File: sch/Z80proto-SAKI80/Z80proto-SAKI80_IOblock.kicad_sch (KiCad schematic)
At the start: 40 parts, among them SW101 RESET, U101 LMC555, U14 AC541, U15 HC139, U17 TD62783, U18 TD62083, U21 23LC512, U4 HC138

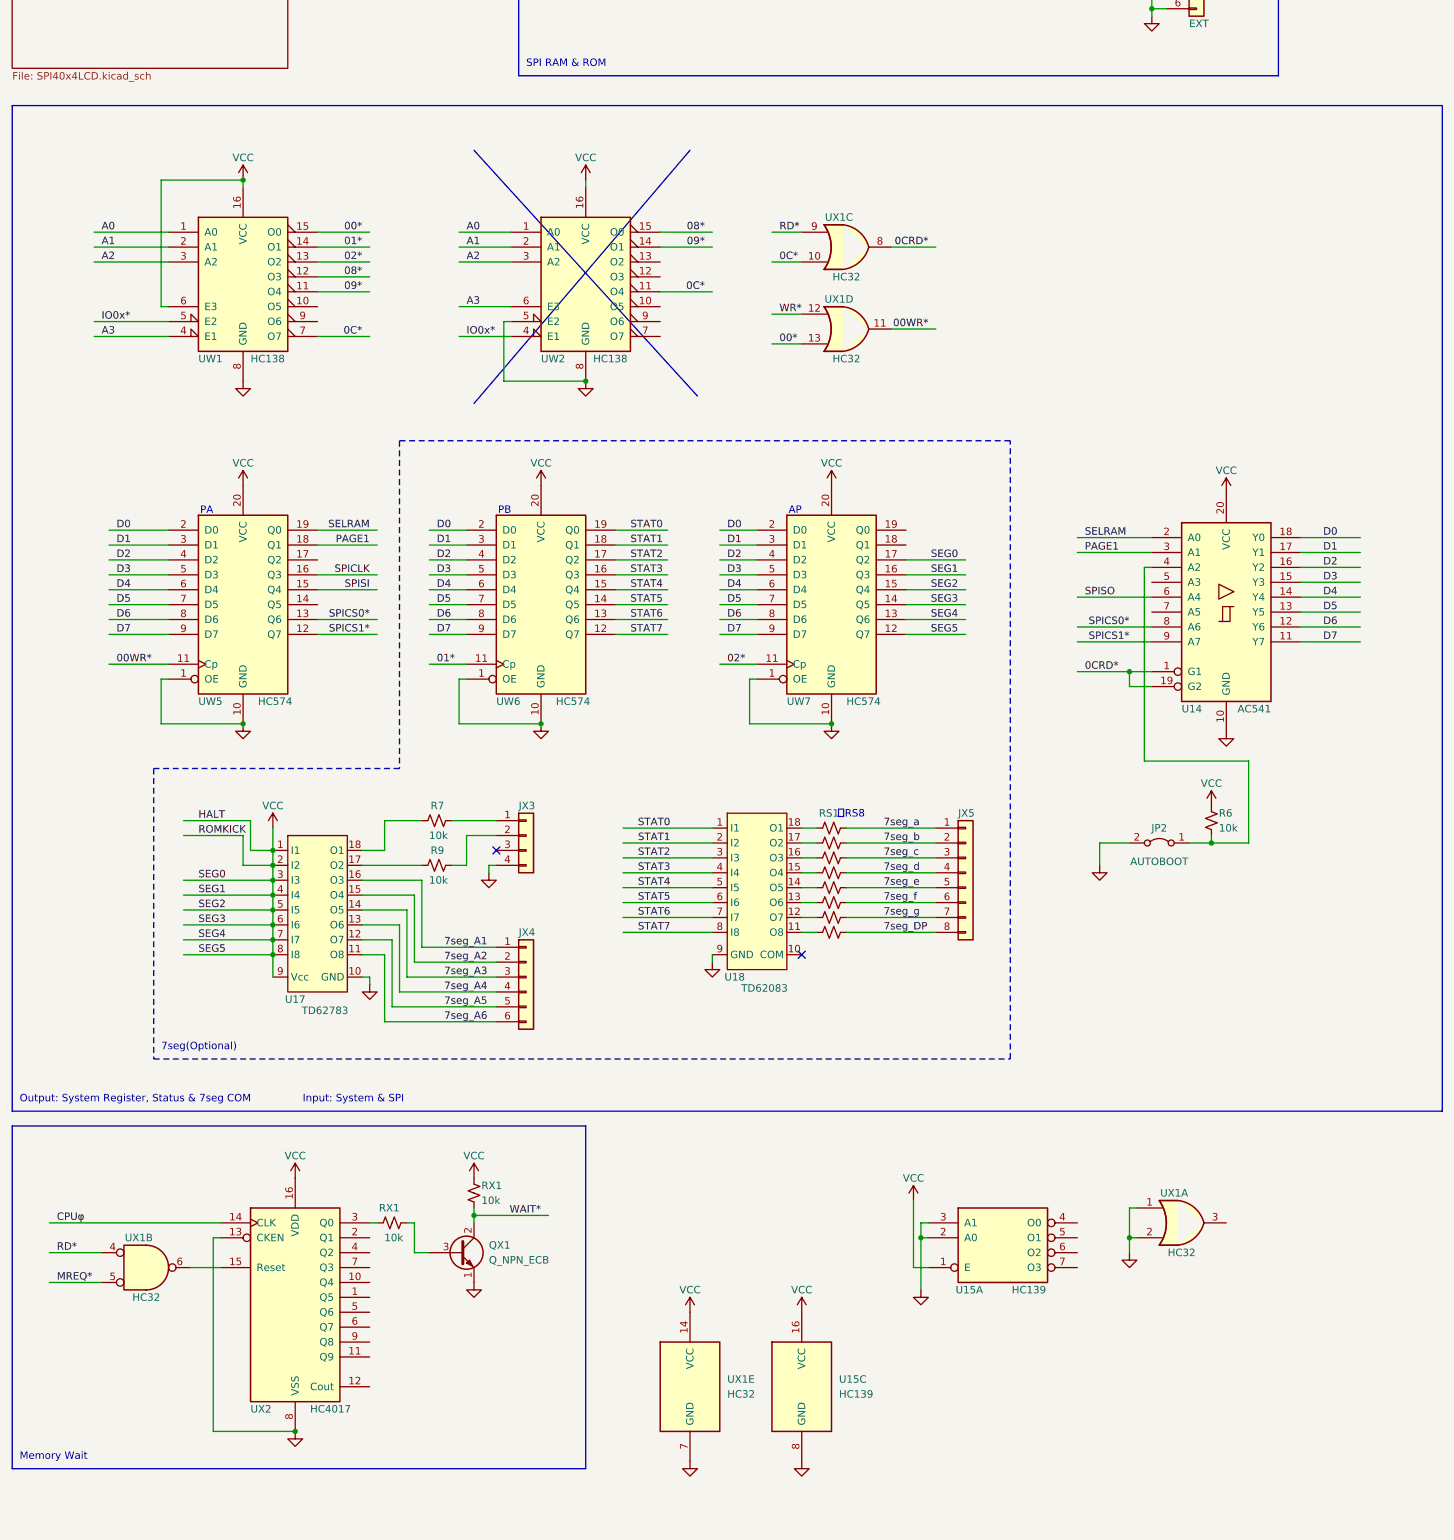
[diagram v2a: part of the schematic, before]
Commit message: Add Async. FIFO support(EXPERIMENTAL)
Add FT245R Asynchronous FIFO support(EXPERIMENTAL)
change environment MiniLoader(zcc->sdcc)
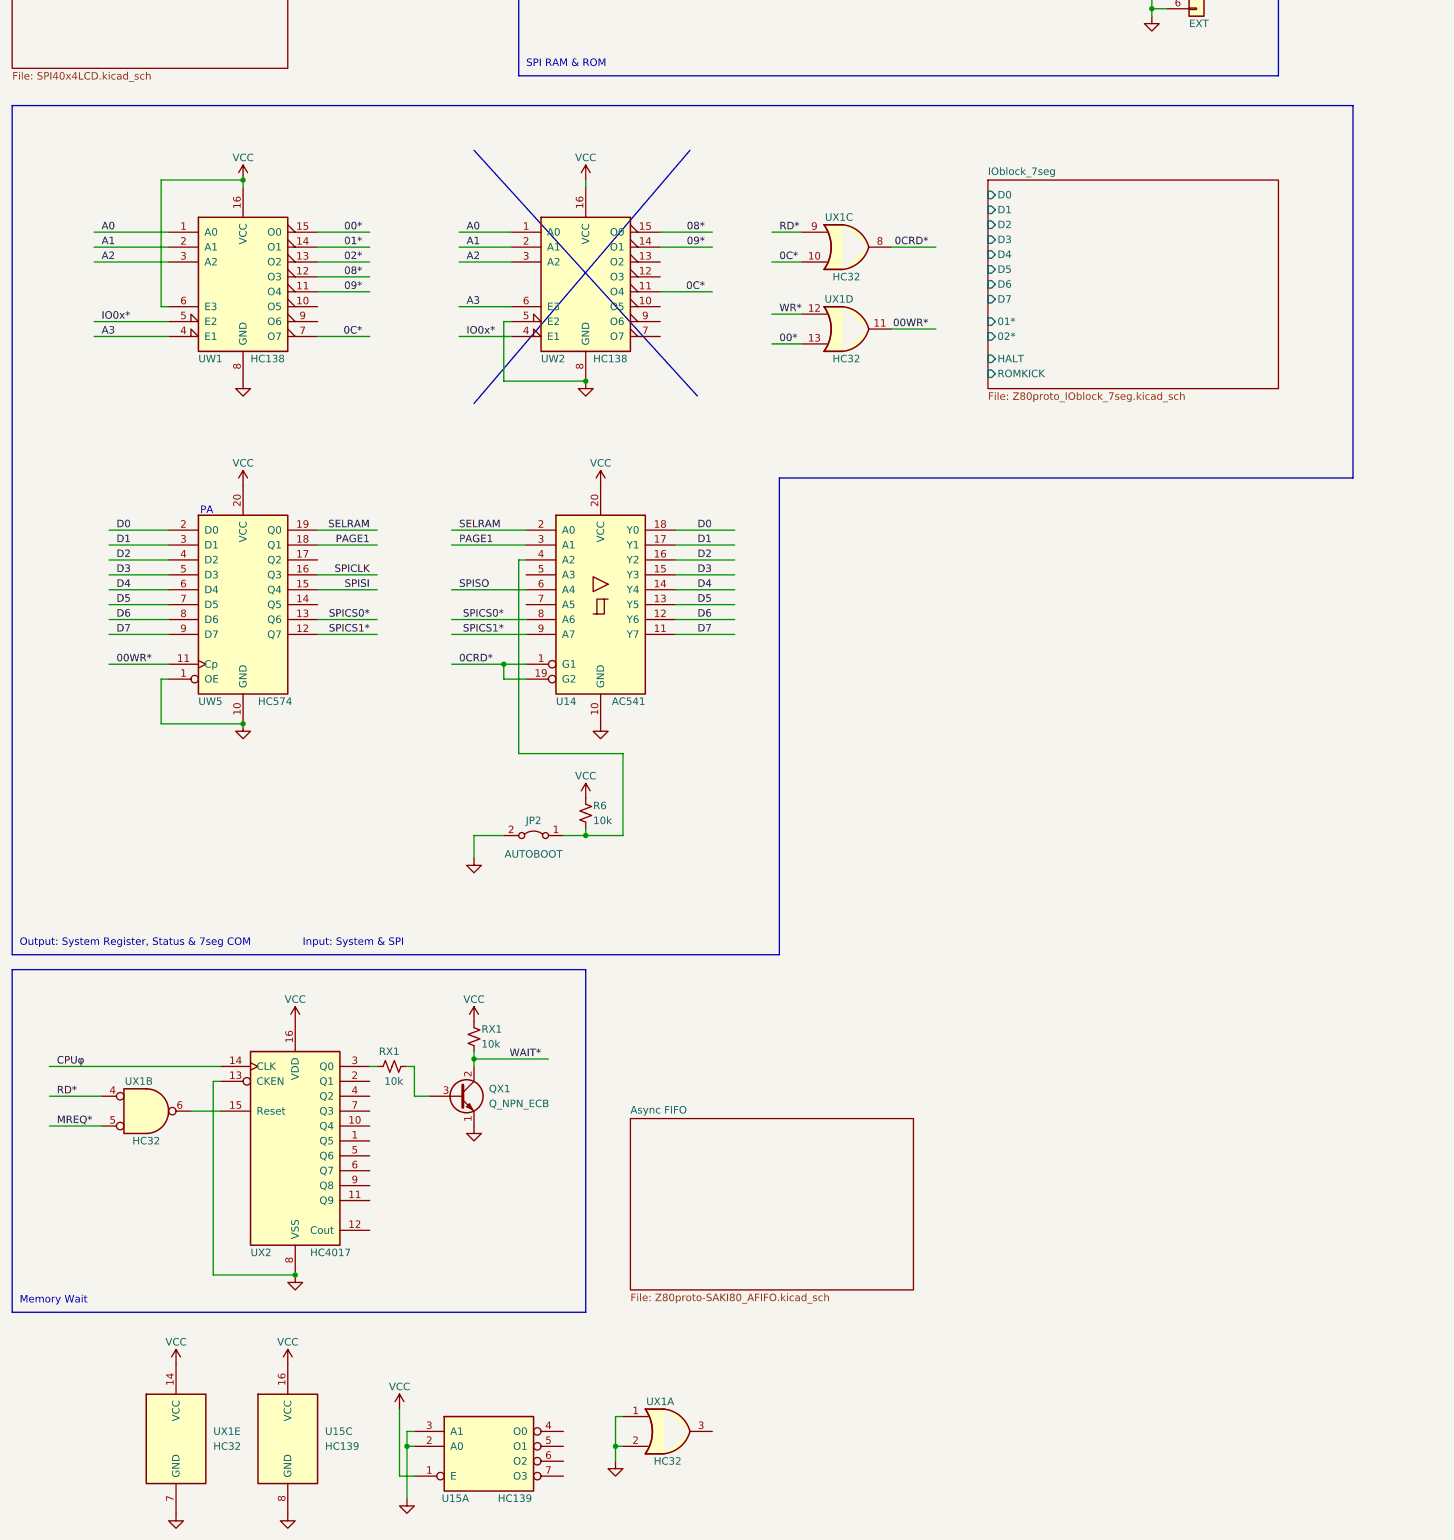
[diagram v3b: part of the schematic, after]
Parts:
- removed JX3: Conn_01x04, symbol Connector_Generic:Conn_01x04
- removed JX4: Conn_01x06, symbol Connector_Generic:Conn_01x06
- removed JX5: Conn_01x08, symbol Connector_Generic:Conn_01x08
- removed R7, R9: 10k, symbol Device:R_Small_US
- removed RS1, RS2, RS3, RS4, RS5, RS6, RS7, RS8: 1k, symbol Device:R_Small_US
- removed U17: TD62783, symbol Toshiba_Sp:TD62783
- removed U18: TD62083, symbol Toshiba_Sp:TD62x83
- removed UW6, UW7: HC574, symbol 74xx:74LS574
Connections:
- no-connect marks 2 -> 0
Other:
- added sheet Async FIFO (Z80proto-SAKI80_AFIFO.kicad_sch)
- added sheet IOblock_7seg (Z80proto_IOblock_7seg.kicad_sch)
- note removed: "7seg(Optional)"
- note removed: "AP"
- note removed: "PB"
- note removed: "～RS8"
- moved on the sheet: JP2, QX1, R6, RX1, U14, U15A, U15C, UX1A, UX1B, UX1E, UX2
